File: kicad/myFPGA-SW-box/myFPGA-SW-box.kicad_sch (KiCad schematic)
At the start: 118 parts, among them J1 Conn_01x04, J10 Conn_01x02, J11 Conn_01x02, J12 Conn_01x02, J2 Conn_01x04, J4 Conn_01x04, J5 Conn_01x04, J6 Conn_01x04, J8 Conn_01x02, U1 74HC595, U10 NC7SB3157P6X, U11 NC7SB3157P6X, U12 NC7SB3157P6X, U13 NC7SB3157P6X, U14 NC7SB3157P6X, U15 NC7SB3157P6X, U16 NC7SB3157P6X, U17 NC7SB3157P6X, U18 NC7SB3157P6X, U19 NC7SB3157P6X, U2 74HC595, U20 NC7SB3157P6X, U21 NC7SB3157P6X, U22 NC7SB3157P6X, U23 NC7SB3157P6X, U24 NC7SB3157P6X, U25 NC7SB3157P6X, U26 NC7SB3157P6X, U27 NC7SB3157P6X, U28 NC7SB3157P6X, U29 NC7SB3157P6X, U3 74HC595, U30 NC7SB3157P6X, U31 NC7SB3157P6X, U32 NC7SB3157P6X, U33 NC7SB3157P6X, U34 NC7SB3157P6X, U35 NC7SB3157P6X, U36 NC7SB3157P6X, U4 74HC595, U5 NC7SB3157P6X, U6 NC7SB3157P6X, U7 NC7SB3157P6X, U8 NC7SB3157P6X, U9 NC7SB3157P6X

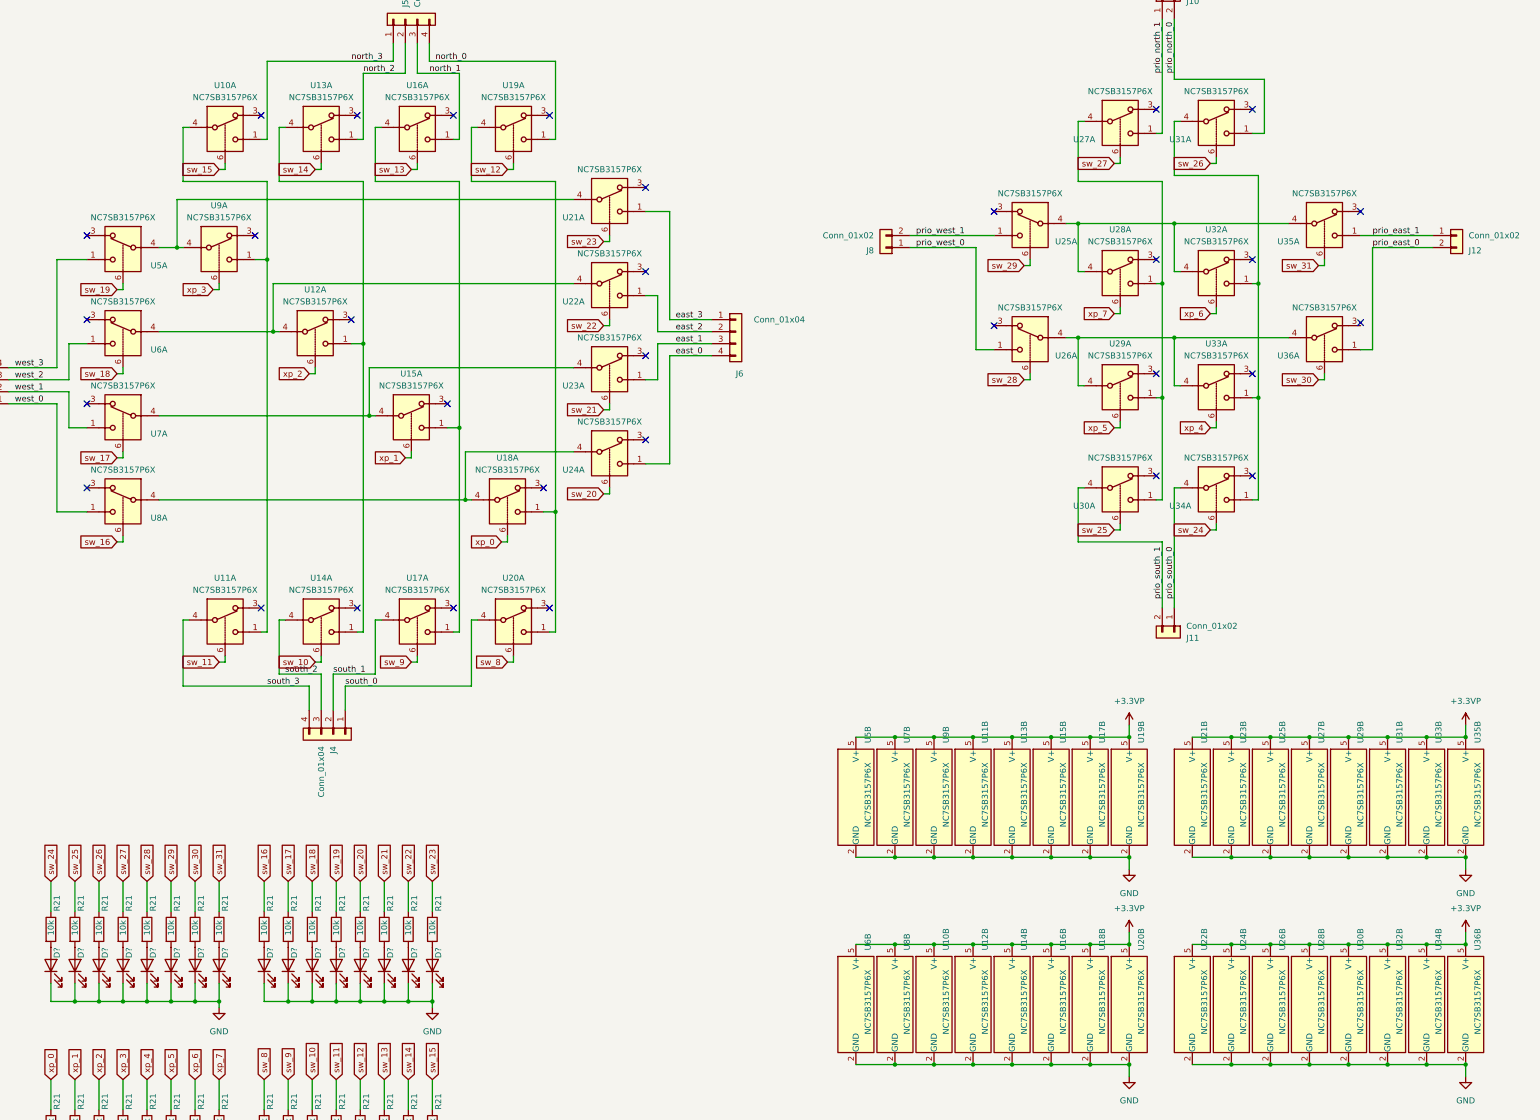
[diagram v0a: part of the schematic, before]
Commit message: CLB slice rev. 2.0 - fix aresetn pullup instead of pulldown - new feature: clock enable - fixes S0 and S1 flipped
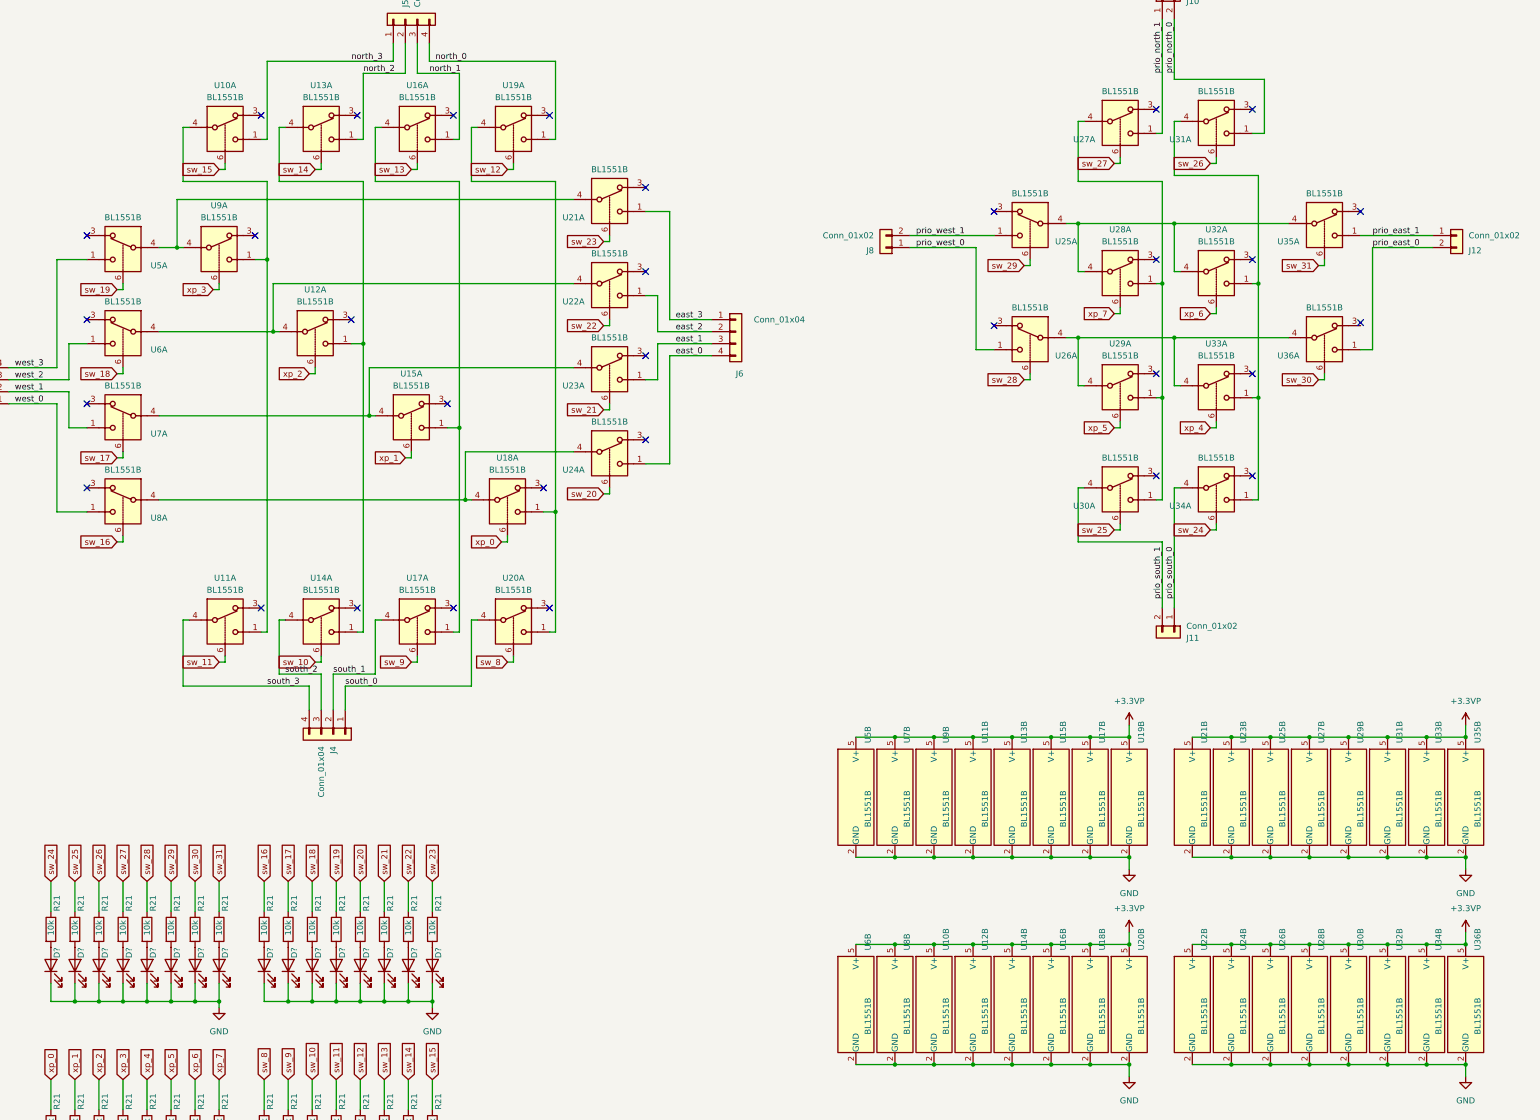
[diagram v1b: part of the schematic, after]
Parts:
- U10, U11, U12, U13, U14, U15, U16, U17, U18, U19, U20, U21, U22, U23, U24, U25, U26, U27, U28, U29, U30, U31, U32, U33, U34, U35, U36, U5, U6, U7, U8, U9: value NC7SB3157P6X -> BL1551B
